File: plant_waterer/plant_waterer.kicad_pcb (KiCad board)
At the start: 2 copper layers, 82.5 x 41.6 mm, 29 parts, among them J2 Conn_01x02, J3 PJ-002AH, J4 Conn_01x03, U1 ZXBM5210-SP-13, U2 OLED_DISP, U4 ESD7002, U5 AP2204R-5.0TRG1, U6 PicoW

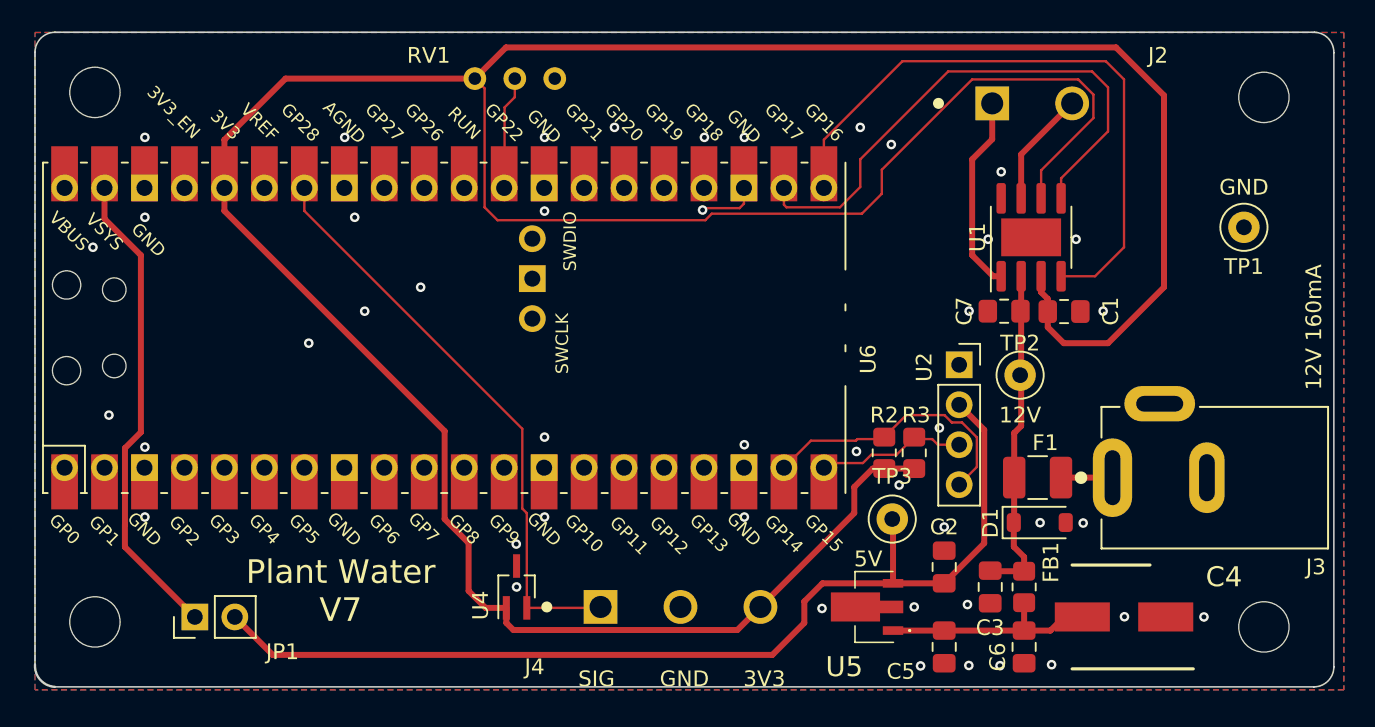
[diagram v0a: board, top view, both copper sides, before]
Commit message: Added off board connectors for I2C
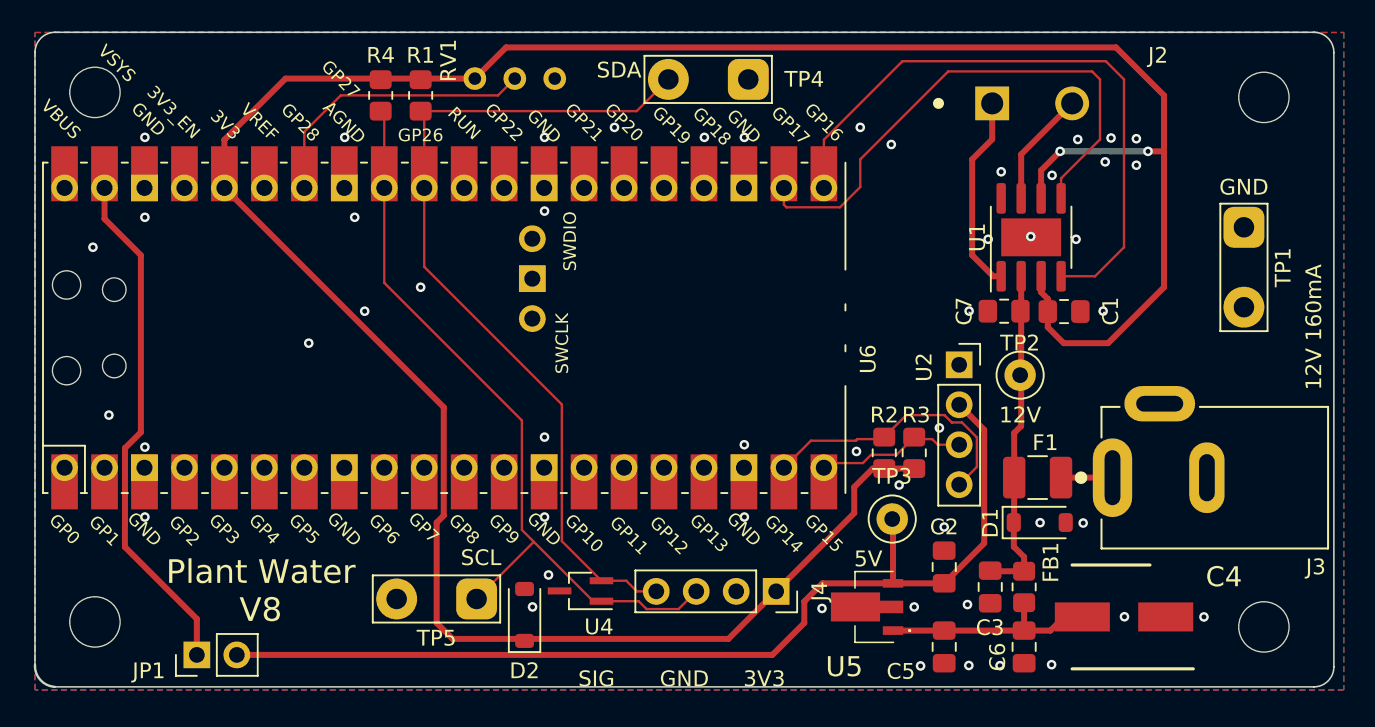
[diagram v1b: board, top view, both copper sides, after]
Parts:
- added D2: TV02W480-G, Diode_SMD:D_SOD-123, F.Cu at (68.6, 71.6)
- added R1: 4K7, Resistor_SMD:R_0805_2012Metric_Pad1.20x1.40mm_HandSolder, F.Cu at (62.0, 38.6)
- added R4: 4K7, Resistor_SMD:R_0805_2012Metric_Pad1.20x1.40mm_HandSolder, F.Cu at (59.4, 38.6)
- added TP4: TestPoint_2Pole, TestPoint:TestPoint_2Pads_Pitch5.08mm_Drill1.3mm, F.Cu at (82.8, 37.6)
- added TP5: TestPoint_2Pole, TestPoint:TestPoint_2Pads_Pitch5.08mm_Drill1.3mm, F.Cu at (65.5, 70.6)
- J4: footprint Library:TE-282841-3-0 -> Connector_PinSocket_2.54mm:PinSocket_1x04_P2.54mm_Vertical
- TP1: footprint TestPoint:TestPoint_Loop_D1.80mm_Drill1.0mm_Beaded -> TestPoint:TestPoint_2Pads_Pitch5.08mm_Drill1.3mm
- moved J4 5.92 mm to (84.6, 70.1), turned to -90 degrees
- moved U4 4.07 mm to (72.1, 70.1), turned to 180 degrees
- moved JP1 2.42 mm to (47.8, 74.2)
- turned TP1 to -90 degrees
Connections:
- J4 pad 1: Net-(J4-Pin_1) -> +3.3V
- J4 pad 3: +3.3V -> /SCL
- RV1 pad 2: Net-(U6-GPIO22) -> Net-(U6-GPIO28_ADC2)
- U4 pad 1: +3.3V -> /SCL
- U4 pad 2: Net-(J4-Pin_1) -> /SDA
- U6 pad 29: Net-(U6-GPIO22) -> unconnected-(U6-GPIO22-Pad29)
- U6 pad 31: unconnected-(U6-GPIO26_ADC0-Pad31) -> /SDA
- U6 pad 32: unconnected-(U6-GPIO27_ADC1-Pad32) -> /SCL
- U6 pad 34: Net-(J4-Pin_1) -> Net-(U6-GPIO28_ADC2)
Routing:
- net /SDA: track 0.00 -> 55.0 mm
- net /SCL: track 0.00 -> 49.1 mm
- net +3.3V: track 219.0 -> 171.3 mm, vias 0 -> 2
- net Net-(J4-Pin_1): track 37.3 -> 0.00 mm
- net Net-(U6-GPIO28_ADC2): track 0.00 -> 18.3 mm
- net Net-(U6-GPIO22): track 7.23 -> 0.00 mm
- net GND: track 5.01 -> 1.21 mm, vias 45 -> 51
- net /5V_JUMP: track 30.5 -> 33.0 mm
- net +5V: track 65.9 -> 64.8 mm
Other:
- board text added: "Plant Water V8"
- board text added: "SCL"
- board text added: "SDA"
- board text removed: "Plant Water V7"

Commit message: Cleanup for V5
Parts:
- added C1: 22nF, Capacitor_SMD:C_0805_2012Metric_Pad1.18x1.45mm_HandSolder, F.Cu at (62.0, 37.6)
- added L1: 100uH, Inductor_SMD:L_0805_2012Metric_Pad1.05x1.20mm_HandSolder, F.Cu at (66.5, 37.6)
- added R1: 100, Resistor_SMD:R_0805_2012Metric_Pad1.20x1.40mm_HandSolder, F.Cu at (70.6, 37.6)
- U4: footprint Package_TO_SOT_SMD:SOT-323_SC-70_Handsoldering -> Package_TO_SOT_SMD:SOT-323_SC-70
- moved R4 35.7 mm to (71.6, 72.2), turned to 90 degrees
- moved R5 35.7 mm to (74.2, 72.1), turned to 90 degrees
- moved RV1 11.6 mm to (53.8, 37.5), turned to 0 degrees
- moved U4 7.08 mm to (78.7, 67.6), turned to 90 degrees
- moved TP5 1.52 mm to (65.5, 69.1)
- moved J3 1.02 mm to (84.6, 71.1)
- renumbered C7 to C2, C1 to C3, C2 to C4, C3 to C5, C4 to C6, C5 to C7, C6 to C8, J2 to J1, J3 to J2, J4 to J3, R1 to R5, TP4 to TP1, TP1 to TP2, TP2 to TP3, TP3 to TP4, U6 to U1, U1 to U2, U2 to U3
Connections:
- U1 pad 16: unconnected-(U6-GPIO12-Pad16) -> /SDA
- U1 pad 17: unconnected-(U6-GPIO13-Pad17) -> /SCL
- U1 pad 31: /SDA -> Net-(U1-GPIO26_ADC0)
- U1 pad 32: /SCL -> unconnected-(U1-GPIO27_ADC1-Pad32)
- U4 pad 1: /SCL -> /SDA
- U4 pad 2: /SDA -> /SCL
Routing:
- net /SCL: track 49.1 -> 25.5 mm
- net /SDA: track 55.0 -> 44.2 mm
- net Net-(U1-GPIO28_ADC2): track 18.3 -> 8.31 mm
- net Net-(U1-GPIO26_ADC0): track 0.00 -> 9.62 mm
- net +3.3V: track 171.3 -> 176.5 mm
- net Net-(L1-Pad1): track 0.00 -> 1.91 mm
- net GND: vias 51 -> 50
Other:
- board text removed: "SIG"

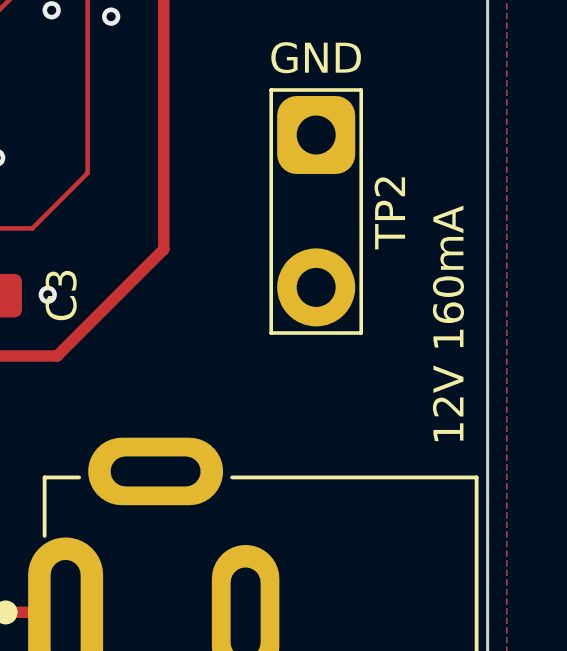
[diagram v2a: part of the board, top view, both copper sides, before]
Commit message: Fixes for footprints
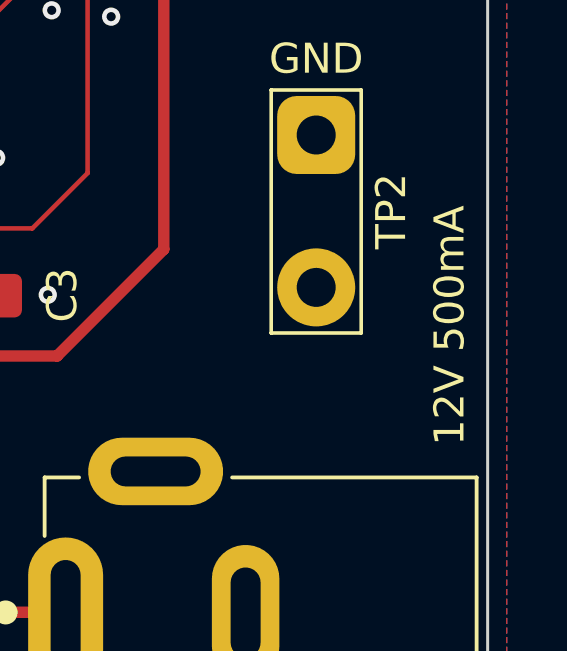
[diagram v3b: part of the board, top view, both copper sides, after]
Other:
- board text added: "12V 500mA"
- board text removed: "12V 160mA"
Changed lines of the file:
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@@
     (effects (font (size 1 1) (thickness 0.15)))
   )
-  (gr_text "12V 160mA" (at 118.745 53.34 90) (layer "F.SilkS")
+  (gr_text "12V 500mA" (at 118.745 53.34 90) (layer "F.SilkS")
     (effects (font (size 1 1) (thickness 0.15)))
   )
